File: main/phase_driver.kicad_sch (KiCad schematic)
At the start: 7 parts, among them Q201 TK4R3E06PL

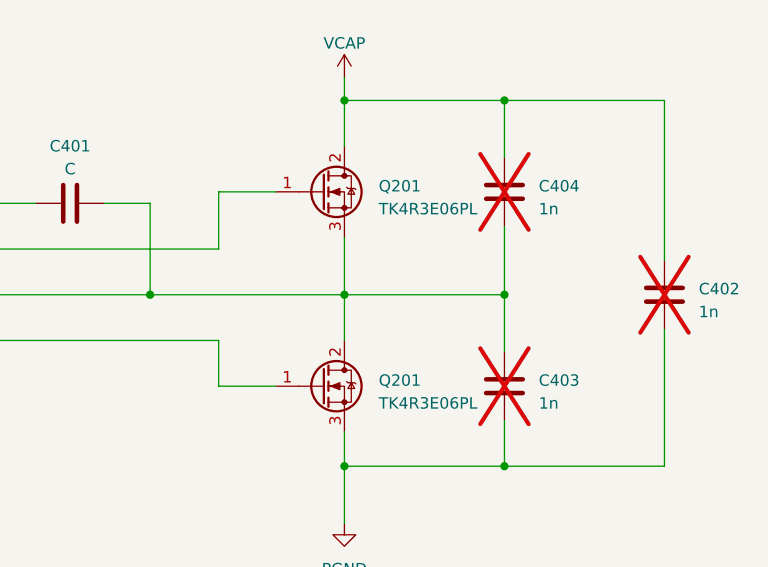
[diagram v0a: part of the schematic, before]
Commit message: Start design of new PSU
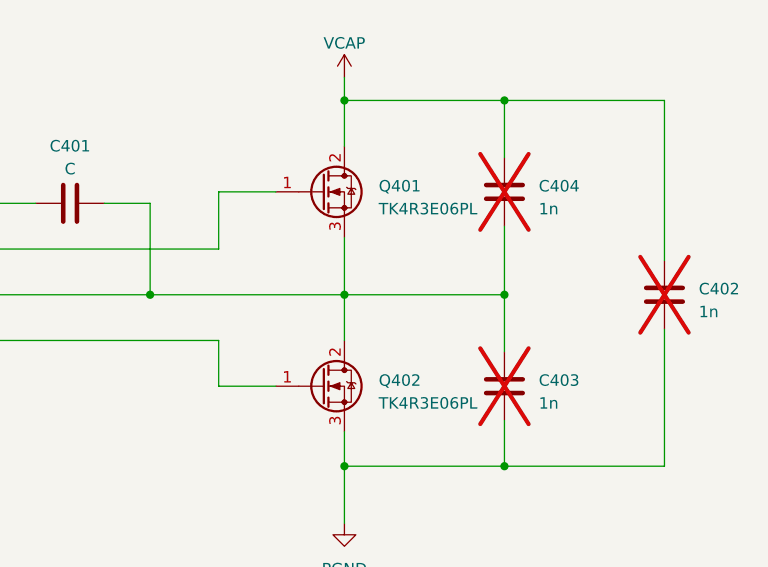
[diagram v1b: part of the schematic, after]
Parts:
- renumbered Q201 to Q401, Q201 to Q402
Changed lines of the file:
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@@
-(kicad_sch (version 20230409) (generator eeschema)
+(kicad_sch (version 20230819) (generator eeschema)
   (paper "A4")
   (junction (at 114.3 80.01) (diameter 0) (color 0 0 0 0)
@@
   )
   (symbol (lib_id "Device:C") (at 83.82 50.8 90) (unit 1)
-    (in_bom yes) (on_board yes) (dnp no) (fields_autoplaced)
+    (exclude_from_sim no) (in_bom yes) (on_board yes) (dnp no) (fields_autoplaced)
     (property "Reference" "C401" (at 83.82 44.45 90)
       (effects (font (size 1.27 1.27)))
@@
       (effects (font (size 1.27 1.27)) hide)
     )
+    (property "Description" "" (at 83.82 50.8 0)
+      (effects (font (size 1.27 1.27)) hide)
+    )
     (pin "1")
     (pin "2")
@@
   )
   (symbol (lib_id "Device:C") (at 132.08 71.12 0) (unit 1)
-    (in_bom no) (on_board yes) (dnp yes) (fields_autoplaced)
+    (exclude_from_sim no) (in_bom no) (on_board yes) (dnp yes) (fields_autoplaced)
     (property "Reference" "C403" (at 135.89 70.485 0)
       (effects (font (size 1.27 1.27)) (justify left))
@@
       (effects (font (size 1.27 1.27)) hide)
     )
+    (property "Description" "" (at 132.08 71.12 0)
+      (effects (font (size 1.27 1.27)) hide)
+    )
     (pin "1")
     (pin "2")
@@
   )
   (symbol (lib_id "power:GND") (at 114.3 86.36 0) (unit 1)
-    (in_bom yes) (on_board yes) (dnp no) (fields_autoplaced)
+    (exclude_from_sim no) (in_bom yes) (on_board yes) (dnp no) (fields_autoplaced)
     (property "Reference" "#PWR0401" (at 114.3 92.71 0)
       (effects (font (size 1.27 1.27)) hide)
@@
       (effects (font (size 1.27 1.27)) hide)
     )
+    (property "Description" "" (at 114.3 86.36 0)
+      (effects (font (size 1.27 1.27)) hide)
+    )
     (pin "1")
     (instances
@@
   )
   (symbol (lib_id "Device:C") (at 149.86 60.96 0) (unit 1)
-    (in_bom no) (on_board yes) (dnp yes) (fields_autoplaced)
+    (exclude_from_sim no) (in_bom no) (on_board yes) (dnp yes) (fields_autoplaced)
     (property "Reference" "C402" (at 153.67 60.325 0)
       (effects (font (size 1.27 1.27)) (justify left))
@@
       (effects (font (size 1.27 1.27)) hide)
     )
+    (property "Description" "" (at 149.86 60.96 0)
+      (effects (font (size 1.27 1.27)) hide)
+    )
     (pin "1")
     (pin "2")
@@
   )
   (symbol (lib_id "dsv4:LM2105") (at 64.77 58.42 0) (unit 1)
-    (in_bom yes) (on_board yes) (dnp no) (fields_autoplaced)
+    (exclude_from_sim no) (in_bom yes) (on_board yes) (dnp no) (fields_autoplaced)
     (property "Reference" "U401" (at 64.77 48.26 0)
       (effects (font (size 1.27 1.27)))
@@
       (effects (font (size 1.27 1.27)) hide)
     )
+    (property "Description" "" (at 64.77 58.42 0)
+      (effects (font (size 1.27 1.27)) hide)
+    )
     (pin "")
     (pin "")
@@
   )
   (symbol (lib_id "Device:Q_NMOS_GDS") (at 111.76 49.53 0) (unit 1)
-    (in_bom yes) (on_board yes) (dnp no)
-    (property "Reference" "Q201" (at 118.11 48.895 0)
+    (exclude_from_sim no) (in_bom yes) (on_board yes) (dnp no)
+    (property "Reference" "Q401" (at 118.11 48.895 0)
       (effects (font (size 1.27 1.27)) (justify left))
     )
@@
     )
     (property "Datasheet" "https://www.mouser.fr/datasheet/2/408/TK4R3E06PL_datasheet_en_20210120-1075493.pdf" (at 111.76 49.53 0)
+      (effects (font (size 1.27 1.27)) hide)
+    )
+    (property "Description" "" (at 111.76 49.53 0)
       (effects (font (size 1.27 1.27)) hide)
     )
@@
   )
   (symbol (lib_id "Device:C") (at 132.08 49.53 0) (unit 1)
-    (in_bom no) (on_board yes) (dnp yes) (fields_autoplaced)
+    (exclude_from_sim no) (in_bom no) (on_board yes) (dnp yes) (fields_autoplaced)
     (property "Reference" "C404" (at 135.89 48.895 0)
       (effects (font (size 1.27 1.27)) (justify left))
@@
       (effects (font (size 1.27 1.27)) hide)
     )
+    (property "Description" "" (at 132.08 49.53 0)
+      (effects (font (size 1.27 1.27)) hide)
+    )
     (pin "1")
     (pin "2")
@@
   )
   (symbol (lib_id "power:+5V") (at 35.56 45.72 0) (unit 1)
-    (in_bom yes) (on_board yes) (dnp no) (fields_autoplaced)
+    (exclude_from_sim no) (in_bom yes) (on_board yes) (dnp no) (fields_autoplaced)
     (property "Reference" "#PWR0403" (at 35.56 49.53 0)
       (effects (font (size 1.27 1.27)) hide)
@@
       (effects (font (size 1.27 1.27)) hide)
     )
+    (property "Description" "" (at 35.56 45.72 0)
+      (effects (font (size 1.27 1.27)) hide)
+    )
     (pin "1")
     (instances
@@
   )
   (symbol (lib_id "power:VCC") (at 114.3 36.83 0) (unit 1)
-    (in_bom yes) (on_board yes) (dnp no) (fields_autoplaced)
+    (exclude_from_sim no) (in_bom yes) (on_board yes) (dnp no) (fields_autoplaced)
     (property "Reference" "#PWR0402" (at 114.3 40.64 0)
       (effects (font (size 1.27 1.27)) hide)
@@
       (effects (font (size 1.27 1.27)) hide)
     )
+    (property "Description" "" (at 114.3 36.83 0)
+      (effects (font (size 1.27 1.27)) hide)
+    )
     (pin "1")
     (instances
@@
   )
   (symbol (lib_id "Device:Q_NMOS_GDS") (at 111.76 71.12 0) (unit 1)
-    (in_bom yes) (on_board yes) (dnp no)
-    (property "Reference" "Q201" (at 118.11 70.485 0)
+    (exclude_from_sim no) (in_bom yes) (on_board yes) (dnp no)
+    (property "Reference" "Q402" (at 118.11 70.485 0)
       (effects (font (size 1.27 1.27)) (justify left))
     )
@@
       (effects (font (size 1.27 1.27)) hide)
     )
+    (property "Description" "" (at 111.76 71.12 0)
+      (effects (font (size 1.27 1.27)) hide)
+    )

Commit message: [PSU] Compute values for LT8710 PSU
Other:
- company: (none) -> Julien FAUCHER
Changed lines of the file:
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@@
 (kicad_sch (version 20230819) (generator eeschema)
   (paper "A4")
+  (title_block
+    (date "2023-04-05")
+    (rev "0.1")
+    (company "Julien FAUCHER")
+    (comment 1 "Defis solaires 2024")
+  )
   (junction (at 114.3 80.01) (diameter 0) (color 0 0 0 0)
   )

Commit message: PSU should be OK
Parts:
- removed Q401, Q402: TK4R3E06PL, Package_TO_SOT_THT:TO-220-3_Horizontal_TabUp, symbol Device:Q_NMOS_GDS
- added C205: 1u, symbol Device:C
- added Q201, Q202: TK4R3E06PL, Package_TO_SOT_THT:TO-220-3_Horizontal_TabUp, symbol Device:Q_NMOS_GDS
- added R202, R501: 100k, symbol Device:R
- C502: renamed from C401; value C -> 100n
- renumbered C404 to C501, C402 to C503, C403 to C504, U401 to U501
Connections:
- net +12V: now also C205.1
- net PGND: now also U501. (VDD), C205.2, Q202.2 (D), R202.2, R501.2
- net VCAP: now also Q201.3 (S)
- net OUT: now reaches C501.2, C502.2, C504.1, U501. (VDD)
- net OUT: now also Q201.2 (D), Q202.3 (S)
- new net: Q202.1 (G), U501. (VDD)
- new net: Q201.1 (G), U501. (VDD)
- new net INH: R501.1, U501. (VDD)
- new net INL: R202.1, U501. (VDD)
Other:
- moved on the sheet: C501, C502, C503, C504, U501

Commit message: Progresses
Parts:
- U501: value ~ -> LM2105
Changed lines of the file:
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@@
 	(text "LM2105"
 		(exclude_from_sim no)
-		(at 30.48 21.59 0)
+		(at 117.602 39.116 0)
 		(effects
 			(font
@@
 		(fields_autoplaced yes)
 		(property "Reference" "U501"
-			(at 121.92 55.88 0)
-			(effects
-				(font
-					(size 1.27 1.27)
-				)
-			)
-		)
-		(property "Value" "~"
-			(at 121.92 69.85 0)
+			(at 121.92 52.07 0)
+			(effects
+				(font
+					(size 1.27 1.27)
+				)
+			)
+		)
+		(property "Value" "LM2105"
+			(at 121.92 54.61 0)
 			(effects
 				(font
@@
 			)
 		)
+		(property "MPN" ""
+			(at 121.92 66.04 0)
+			(effects
+				(font
+					(size 1.27 1.27)
+				)
+			)
+		)
+		(property "Name" ""
+			(at 121.92 66.04 0)
+			(effects
+				(font
+					(size 1.27 1.27)
+				)
+			)
+		)
 		(pin ""
 		)
@@
 				(path "/c07e9297-fde8-4755-803e-d05072cd6096/bed5353e-e607-4c1c-98ea-22040242af2e/a3c0ac15-b403-4abe-8c9f-dc79c64677cd"
 					(reference "#PWR01105")
+					(unit 1)
+				)
+				(path "/c07e9297-fde8-4755-803e-d05072cd6096/5b9a617b-6d93-4d9f-bce1-510d294da22c/cee9b468-980d-45cd-b1b7-f04fc6f76443"
+					(reference "#PWR0205")
 					(unit 1)
 				)
@@
 					(unit 1)
 				)
+				(path "/c07e9297-fde8-4755-803e-d05072cd6096/5b9a617b-6d93-4d9f-bce1-510d294da22c/cee9b468-980d-45cd-b1b7-f04fc6f76443"
+					(reference "R202")
+					(unit 1)
+				)
 			)
 		)
@@
 					(unit 1)
 				)
+				(path "/c07e9297-fde8-4755-803e-d05072cd6096/5b9a617b-6d93-4d9f-bce1-510d294da22c/cee9b468-980d-45cd-b1b7-f04fc6f76443"
+					(reference "C205")
+					(unit 1)
+				)

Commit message: Update schematics
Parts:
- added D202, D501: D_Schottky, symbol Device:D_Schottky
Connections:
- net OUT: now also D202.1 (K), D501.2 (A)
- net PGND: now also D202.2 (A)
- net VCAP: now also D501.1 (K)
- net +12V renamed V_{DRIVE}
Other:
- moved on the sheet: C501, C503, C504

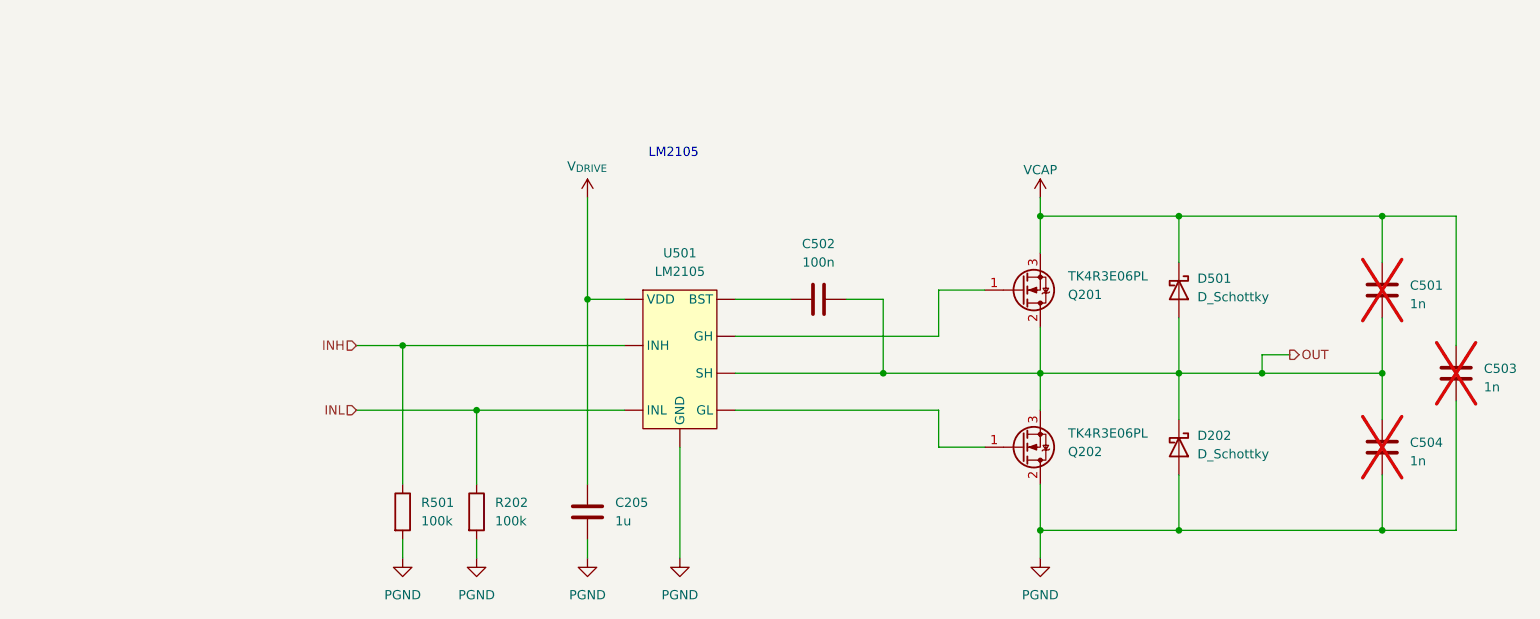
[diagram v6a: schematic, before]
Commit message: Finalize sch and start component mapping
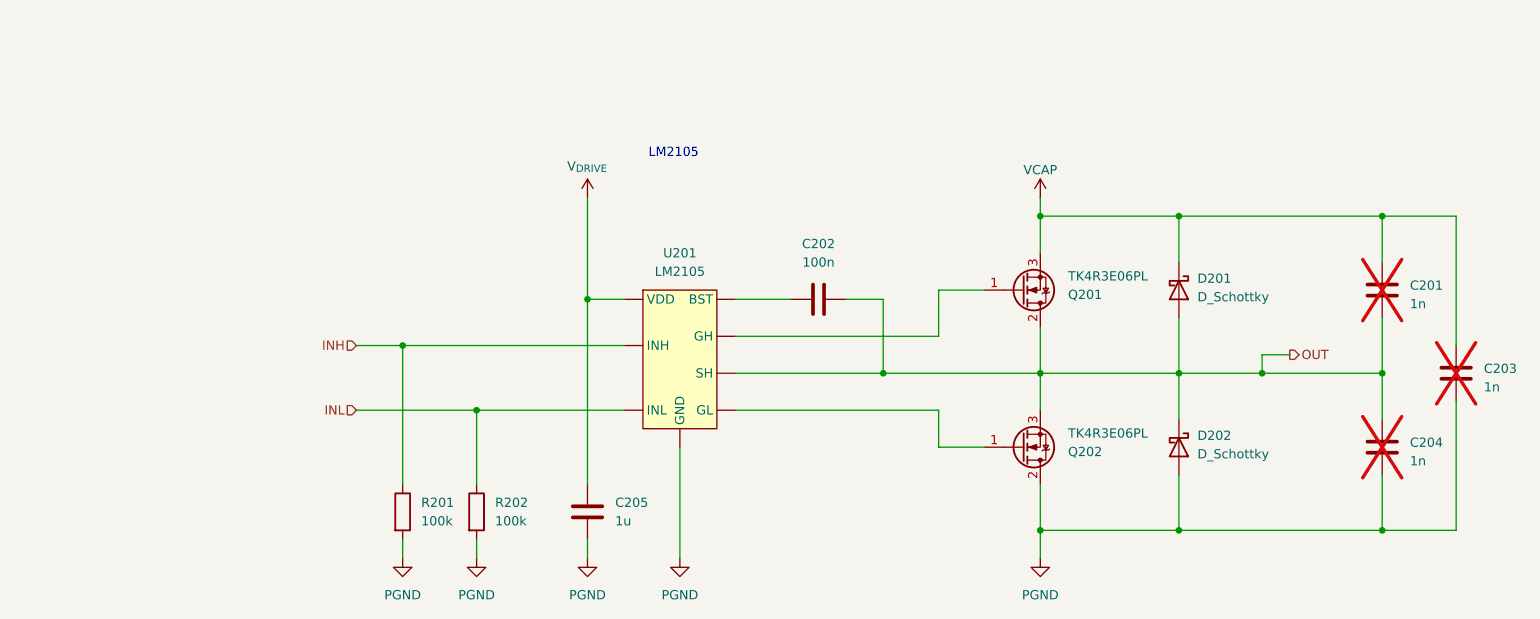
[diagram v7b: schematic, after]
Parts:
- C201: renamed from C501; footprint (none) -> Capacitor_SMD:C_0805_2012Metric
- C202: renamed from C502; footprint (none) -> Capacitor_SMD:C_0805_2012Metric
- C203: renamed from C503; footprint (none) -> Capacitor_SMD:C_0805_2012Metric
- C204: renamed from C504; footprint (none) -> Capacitor_SMD:C_0805_2012Metric
- C205: footprint (none) -> Capacitor_SMD:C_0805_2012Metric
- R201: renamed from R501; footprint (none) -> Resistor_SMD:R_0805_2012Metric
- R202: footprint (none) -> Resistor_SMD:R_0805_2012Metric
- renumbered D501 to D201, U501 to U201

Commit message: BOM OK
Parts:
- D201, D202: value D_Schottky -> B5819W-TP; footprint (none) -> Diode_SMD:D_SOD-123
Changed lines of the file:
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@@
 			)
 		)
-		(property "Value" "D_Schottky"
+		(property "Value" " B5819W-TP "
 			(at 193.04 58.1024 90)
 			(effects
@@
 			)
 		)
-		(property "Footprint" ""
+		(property "Footprint" "Diode_SMD:D_SOD-123"
 			(at 190.5 57.15 0)
 			(effects
@@
 			)
 		)
-		(property "Value" "D_Schottky"
+		(property "Value" " B5819W-TP "
 			(at 193.04 79.6924 90)
 			(effects
@@
 			)
 		)
-		(property "Footprint" ""
+		(property "Footprint" "Diode_SMD:D_SOD-123"
 			(at 190.5 78.74 0)
 			(effects
